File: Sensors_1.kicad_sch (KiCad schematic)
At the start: 27 parts, among them J7 Conn_01x04_Pin, J8 Conn_01x06_Pin, J9 Conn_01x02_Pin, U3 Ai-Thinker-Ra-01

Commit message: feat: доработана схема питания, расчечены габариты печатной платы
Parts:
- removed C31: 0.1u, Capacitor_SMD:C_0805_2012Metric_Pad1.18x1.45mm_HandSolder, symbol Device:C_Small
- removed D7, D8: SMBJ5.0CA, Diode_SMD:D_SMB_Handsoldering, symbol TVS:SMBJ5.0CA
- removed L2: BLM21PG121SN1D, Inductor_SMD:L_0805_2012Metric_Pad1.05x1.20mm_HandSolder, symbol Inductors:L
- added D4, D5: SMAJ5.0CA, Diode_SMD:D_SMA, symbol Diode:SMAJ5.0CA
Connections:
- net +3V3D: now also C32.1, U3.3 (VDD)
- net +5V: now also D4.2 (A2), D5.2 (A2)
- net GND: now also D4.1 (A1), D5.1 (A1)
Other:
- moved on the sheet: C27, J7, VD1

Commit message: feat: Добавил внешние интерфейсы
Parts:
- removed C27, C28: 0.1u, Capacitor_SMD:C_0805_2012Metric_Pad1.18x1.45mm_HandSolder, symbol Device:C_Small
- removed D4, D5: SMAJ5.0CA, Diode_SMD:D_SMA, symbol Diode:SMAJ5.0CA
- removed J7: Conn_01x04_Pin, Connector_PinHeader_2.54mm:PinHeader_1x04_P2.54mm_Horizontal, symbol Connector:Conn_01x04_Pin
- removed J8: Conn_01x06_Pin, Connector_Hirose:Hirose_DF13-06P-1.25DSA_1x06_P1.25mm_Vertical, symbol Connector:Conn_01x06_Pin
- removed J9: Conn_01x02_Pin, Connector_Hirose:Hirose_DF13-02P-1.25DSA_1x02_P1.25mm_Vertical, symbol Connector:Conn_01x02_Pin
- removed R7, R8: 3.3k, Resistor_SMD:R_0805_2012Metric_Pad1.20x1.40mm_HandSolder, symbol Device:R
- removed VD1, VD2, VD3: GSOT03C-E3-08, Package_TO_SOT_SMD:SOT-23_Handsoldering, symbol TWS:GSOT03C-E3-08
- added C48: 0.1u, Capacitor_SMD:C_0805_2012Metric_Pad1.18x1.45mm_HandSolder, symbol Device:C_Small
- added U9: Ai-Thinker-Ra-01, RF_Module:Ai-Thinker-Ra-01-LoRa, symbol Receiver_and_transmitter:Ai-Thinker-Ra-01
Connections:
- net +3V3D: now also C48.1, U9.3 (VDD)
- net GND: now also C48.2, U9.16 (GND), U9.2 (GND), U9.9 (GND)
- new net DIO0_RaSH: U9.5 (DIO0)
- new net DIO1_RaSH: U9.6 (DIO1)
- new net DIO2_RaSH: U9.7 (DIO2)
- new net MISO_RaSH: U9.13 (MISO)
- new net MOSI_RaSH: U9.14 (MOSI)
- new net Reset_RaSH: U9.4 (~{RESET})
- new net SCK_RaSH: U9.12 (SCK)
- new net SS_RaSH: U9.15 (~{NSS})
- no-connect marks 8 -> 10

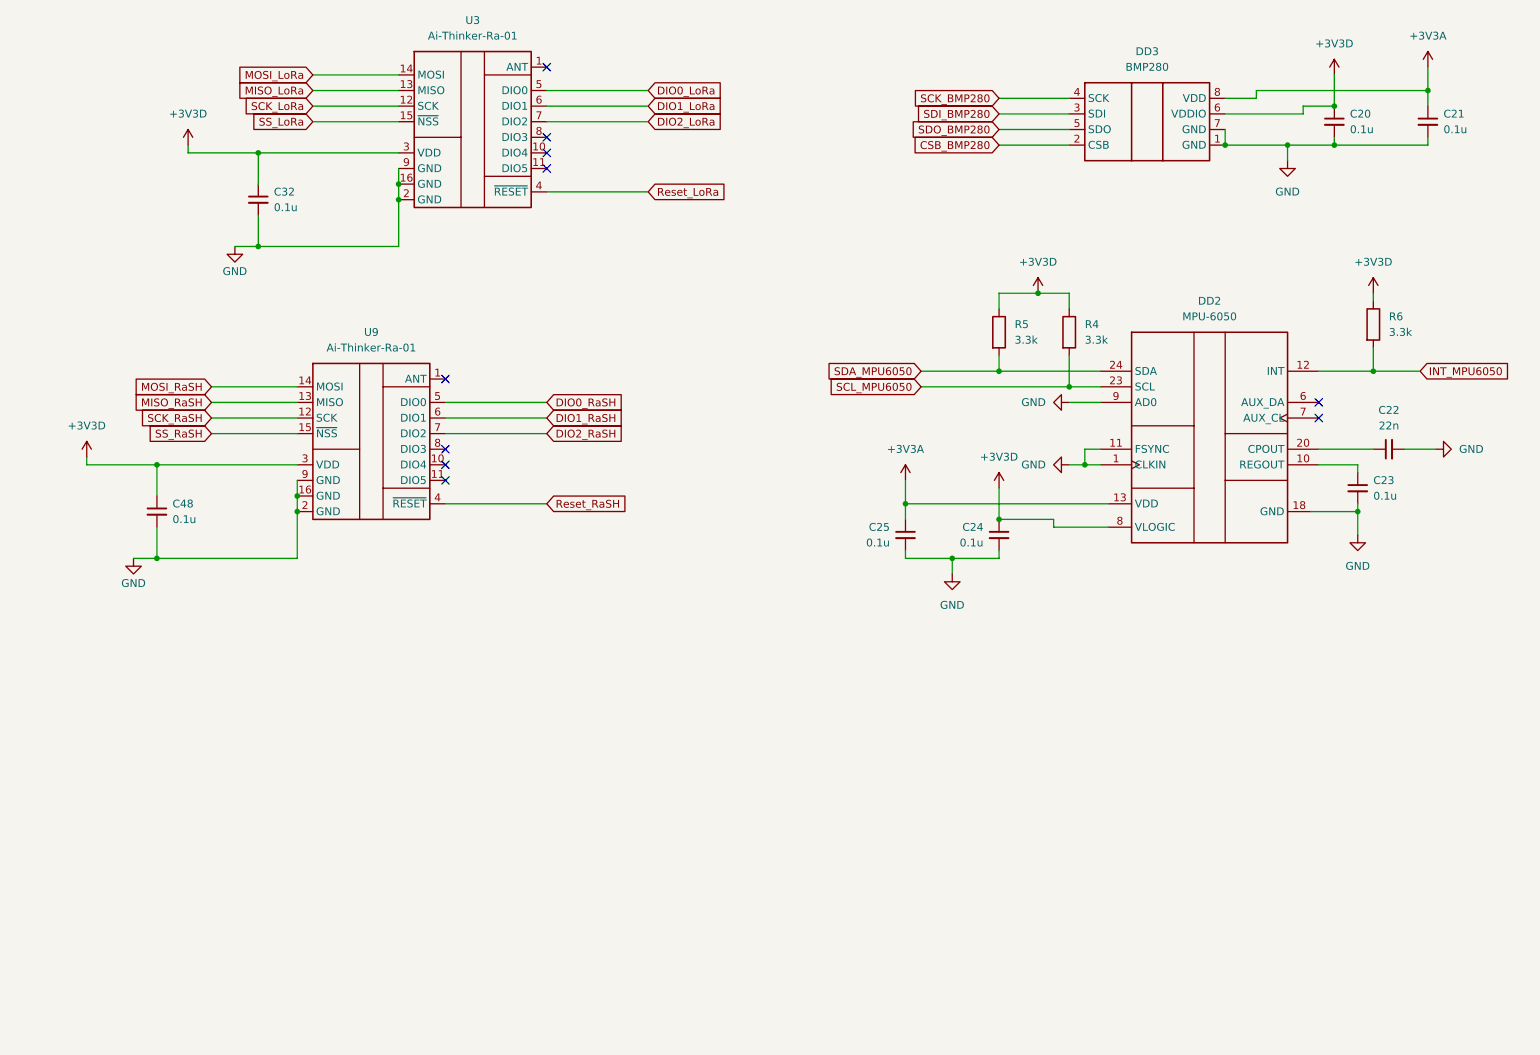
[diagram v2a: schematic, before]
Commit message: feat: добавлены все элементы схемы, начал соединение сигнгальных линий к микроконтроллеру
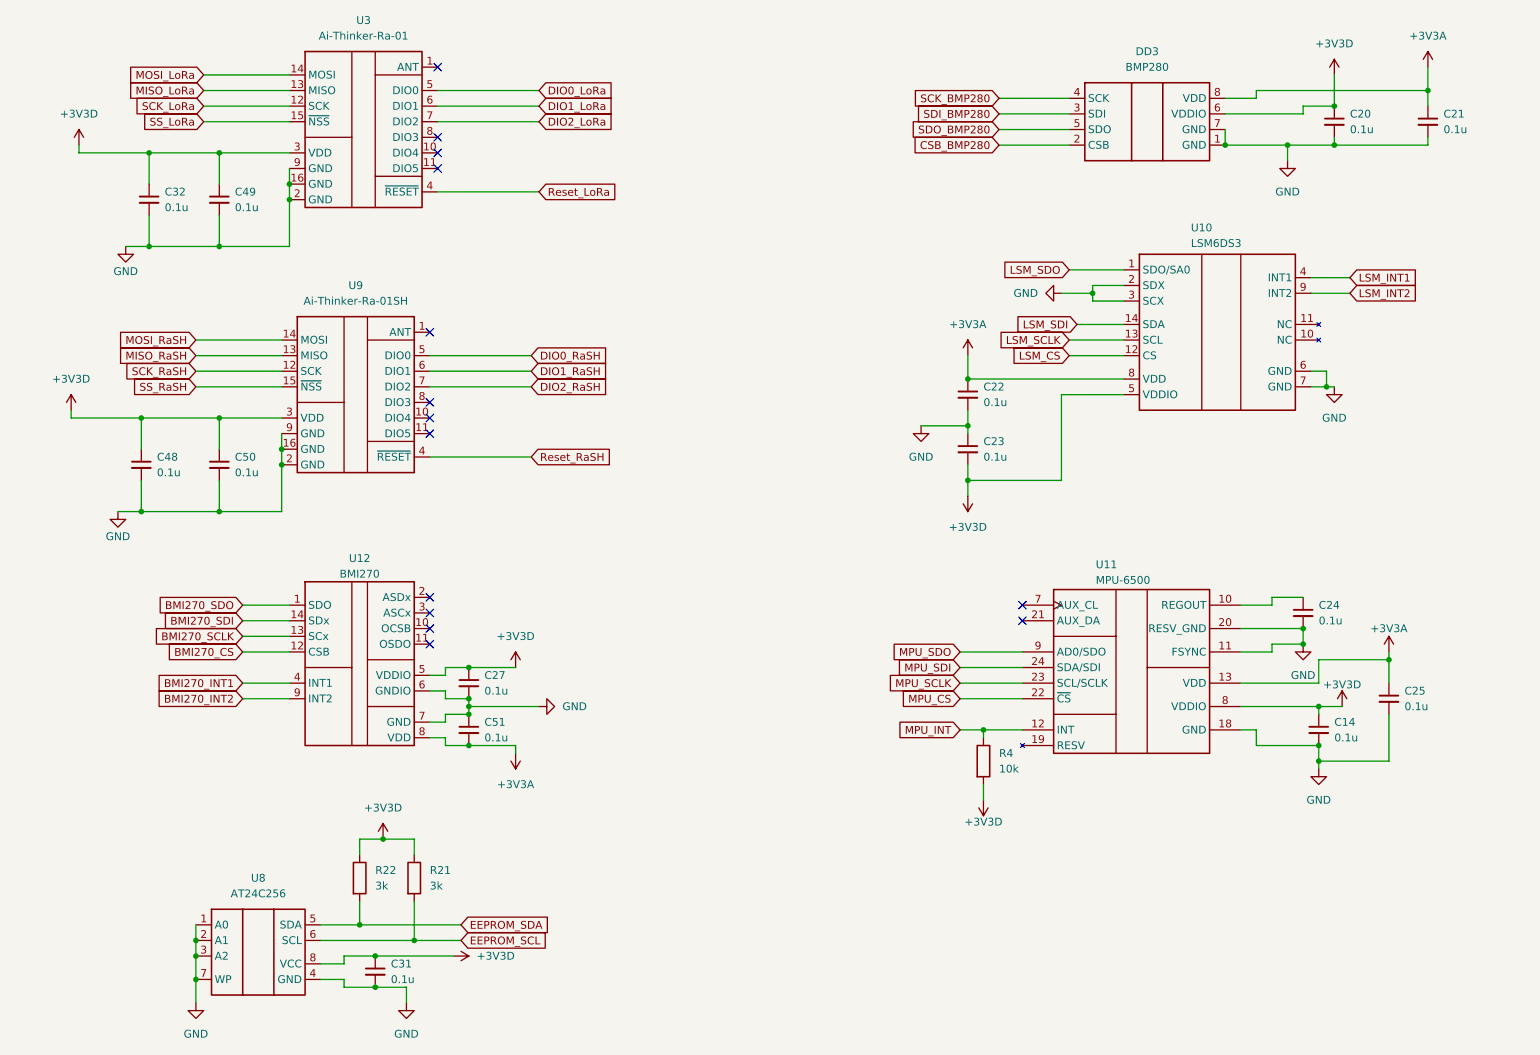
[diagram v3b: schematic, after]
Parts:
- removed DD2: MPU-6050, Sensor_Motion:InvenSense_QFN-24_4x4mm_P0.5mm, symbol Sensors:MPU-6050
- removed R5, R6: 3.3k, Resistor_SMD:R_0805_2012Metric_Pad1.20x1.40mm_HandSolder, symbol Device:R
- added C14, C27, C31, C49, C50, C51: 0.1u, Capacitor_SMD:C_0805_2012Metric_Pad1.18x1.45mm_HandSolder, symbol Device:C_Small
- added R21, R22: 3k, Resistor_SMD:R_0805_2012Metric_Pad1.20x1.40mm_HandSolder, symbol Device:R
- added U10: LSM6DS3, Package_LGA:LGA-14_3x2.5mm_P0.5mm_LayoutBorder3x4y, symbol Sensor_Motion:LSM6DS3
- added U11: MPU-6500, Sensor_Motion:InvenSense_QFN-24_3x3mm_P0.4mm, symbol Sensor_Motion:MPU-9250
- added U12: BMI270, Package_LGA:Bosch_LGA-14_3x2.5mm_P0.5mm, symbol IMU:BMI270
- added U8: AT24C256, Package_SO:SOIC-8_3.9x4.9mm_P1.27mm, symbol EEPROM:AT24C256
- C22: value 22n -> 0.1u
- R4: value 3.3k -> 10k
- U9: value Ai-Thinker-Ra-01 -> Ai-Thinker-Ra-01SH
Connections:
- net SCL_MPU6050 is gone; now on net +3V3D: R4.2
- net +3V3A: now also C22.1, C51.2, U10.8 (VDD), U11.13 (VDD), U12.8 (VDD)
- net +3V3D: now also C23.2, C14.1, C27.1, C31.1, C49.1, C50.1, R21.1, R22.1, U10.5 (VDDIO), U11.8 (VDDIO), U12.5 (VDDIO), U8.8 (VCC); no longer C24.1, R4.1
- net GND: now also C23.1, C14.2, C27.2, C31.2, C49.2, C50.2, C51.1, U10.2 (SDX), U10.3 (SCX), U10.6 (GND), U10.7 (GND), U11.11 (FSYNC), U11.18 (GND), U11.20 (RESV_GND), U12.6 (GNDIO), U12.7 (GND), U8.1 (A0), U8.2 (A1), U8.3 (A2), U8.4 (GND), U8.7 (WP); no longer C23.2
- new net: C24.1, U11.10 (REGOUT)
- new net: U11.1 (NC), U11.2 (NC), U11.3 (NC), U11.4 (NC), U11.5 (NC), U11.6 (NC)
- new net BMI270_CS: U12.12 (CSB)
- new net BMI270_INT1: U12.4 (INT1)
- new net BMI270_INT2: U12.9 (INT2)
- new net BMI270_SCLK: U12.13 (SCx)
- new net BMI270_SDI: U12.14 (SDx)
- new net BMI270_SDO: U12.1 (SDO)
- new net EEPROM_SCL: R21.2, U8.6 (SCL)
- new net EEPROM_SDA: R22.2, U8.5 (SDA)
- new net LSM_CS: U10.12 (CS)
- new net LSM_INT1: U10.4 (INT1)
- new net LSM_INT2: U10.9 (INT2)
- new net LSM_SCLK: U10.13 (SCL)
- new net LSM_SDI: U10.14 (SDA)
- new net LSM_SDO: U10.1 (SDO/SA0)
- new net MPU_CS: U11.22 (~{CS})
- new net MPU_INT: R4.1, U11.12 (INT)
- new net MPU_SCLK: U11.23 (SCL/SCLK)
- new net MPU_SDI: U11.24 (SDA/SDI)
- new net MPU_SDO: U11.9 (AD0/SDO)
- no-connect marks 10 -> 14
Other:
- moved on the sheet: C32, C48, U3, U9
